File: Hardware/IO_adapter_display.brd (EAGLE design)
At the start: 67.3 x 41.9 mm, 23 parts, among them Y1 32Khz

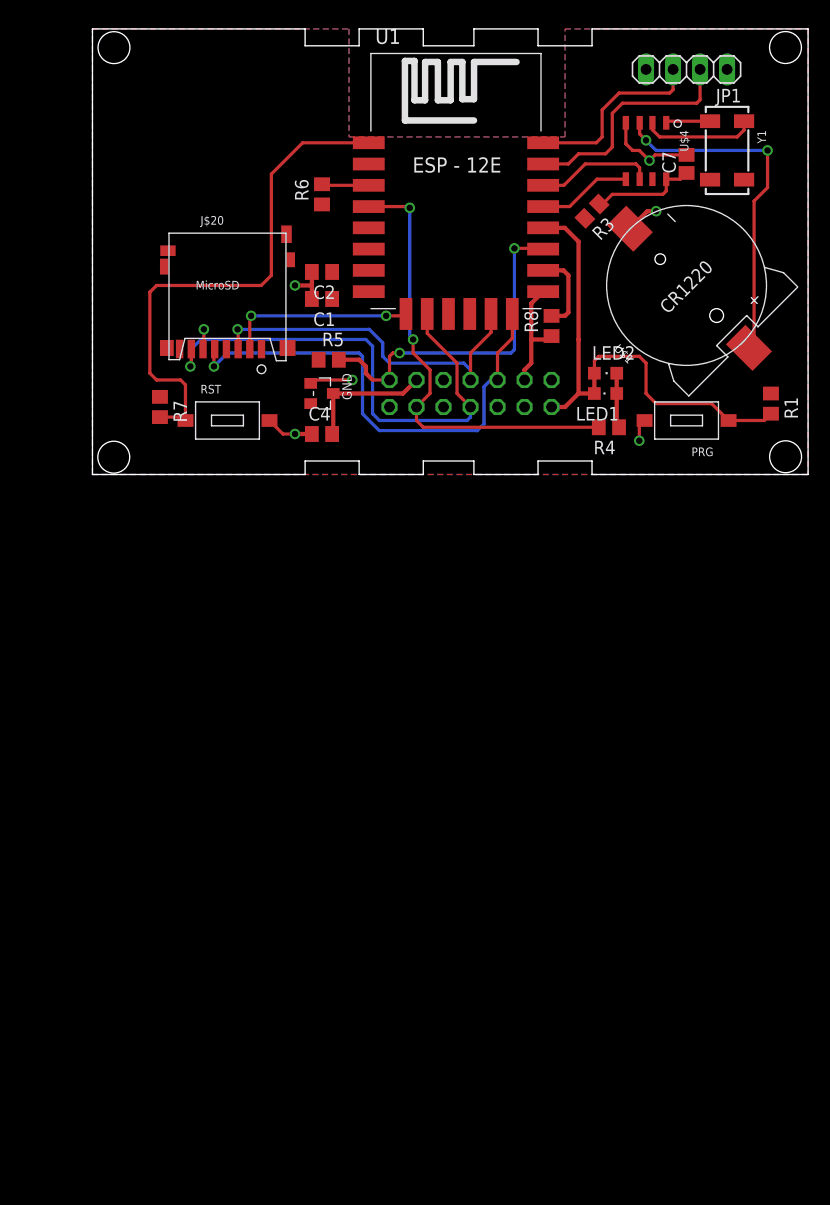
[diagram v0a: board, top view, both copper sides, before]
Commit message: beginning to add a 2.2" TFT display
not quite sure about the mechanical layout yet.
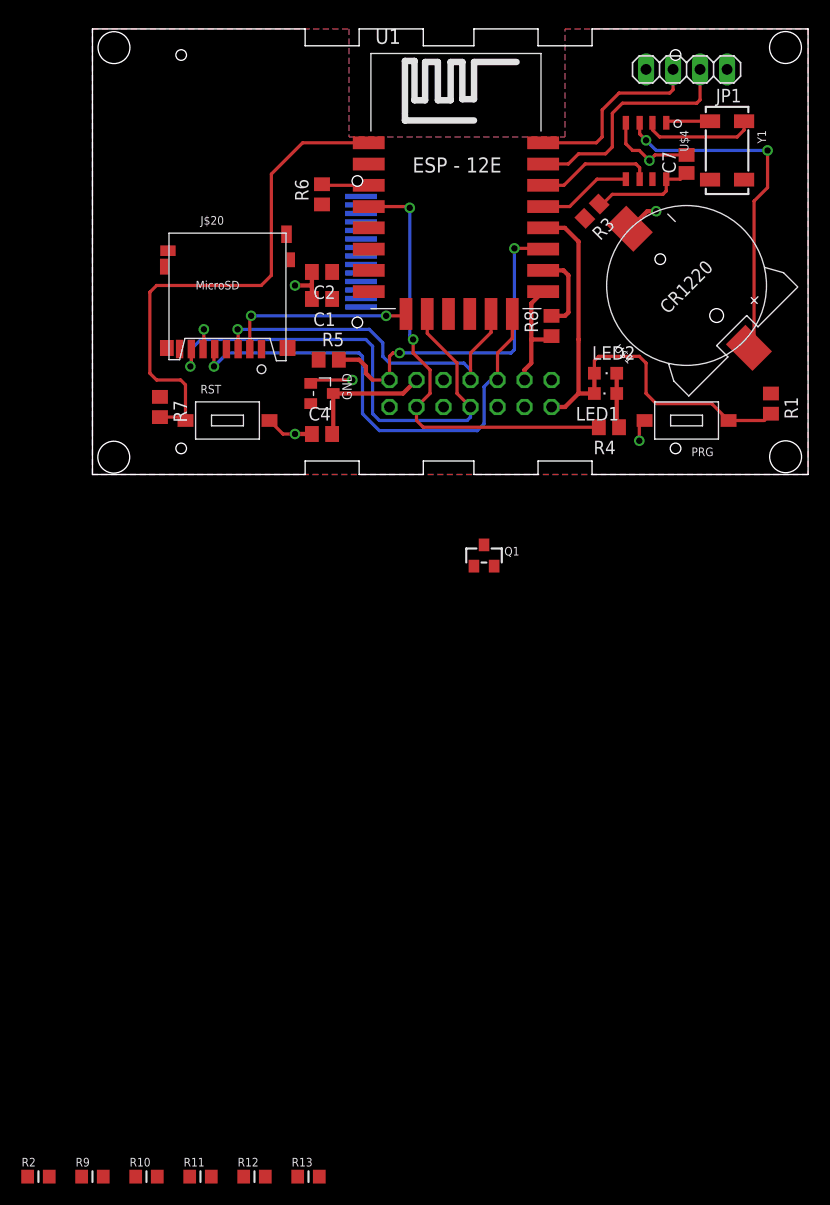
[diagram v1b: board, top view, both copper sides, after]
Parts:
- added Q1: 2N2222, microbuilder:SOT23-WIDE
- added R10, R13, R2, R9: 10, microbuilder:_0805MP
- added R11: 1K, microbuilder:_0805MP
- added R12: 10K, microbuilder:_0805MP
- added U2: (no value), microbuilder:TM022HDH26_2.2IN_LCD
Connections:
- new net 3.3V: R12.2, U2.10, U2.9
- new net BACKLIGHT: R11.1, R12.1
- new net DC_3V: U2.4
- new net LCDCS_3V: U2.5
- new net LEDK: Q1.3, R10.1, R13.1, R2.1, R9.1
- new net MOSI_3V: U2.6
- new net N$2: R2.2, U2.11
- new net N$3: R9.2, U2.12
- new net N$4: R10.2, U2.13
- new net N$5: Q1.1, R11.2
- new net N$6: R13.2, U2.14
- new net RESET_3V: U2.2
- new net SCLK_3V: U2.3
- net GND: now also Q1.2, U2.1, U2.8
- net MISO: now also U2.7
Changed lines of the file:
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@@
 <element name="RST" library="tactile_switch" package="TACT_6X3.5" value="6X3.5_TACT" x="12.7" y="5.08"/>
 <element name="JP1" library="pinhead" package="1X04" value="" x="55.88" y="38.1" rot="R180"/>
+<element name="R2" library="microbuilder" package="_0805MP" value="10" x="-5.08" y="-66.04"/>
+<element name="R9" library="microbuilder" package="_0805MP" value="10" x="0" y="-66.04"/>
+<element name="R10" library="microbuilder" package="_0805MP" value="10" x="5.08" y="-66.04"/>
+<element name="Q1" library="microbuilder" package="SOT23-WIDE" value="2N2222" x="36.83" y="-7.62"/>
+<element name="R11" library="microbuilder" package="_0805MP" value="1K" x="10.16" y="-66.04"/>
+<element name="R12" library="microbuilder" package="_0805MP" value="10K" x="15.24" y="-66.04"/>
+<element name="U2" library="microbuilder" package="TM022HDH26_2.2IN_LCD" value="" x="34.925" y="20.955" rot="MR90"/>
+<element name="R13" library="microbuilder" package="_0805MP" value="10" x="20.32" y="-66.04"/>
 </elements>
 <signals>
@@
 <wire x1="52.187690625" y1="24.765" x2="53.0225" y2="24.765" width="0.4064" layer="1"/>
 <via x="53.0225" y="24.765" extent="1-16" drill="0.6" shape="octagon"/>
-<wire x1="33.02" y1="6.35" x2="40.64" y2="6.35" width="0" layer="19" extent="1-1"/>
+<contactref element="U2" pad="1"/>
+<contactref element="U2" pad="8"/>
+<contactref element="Q1" pad="2"/>
+<wire x1="50.17" y1="33.08" x2="52.07" y2="38.1" width="0" layer="19" extent="1-1"/>
+<wire x1="52.187690625" y1="24.765" x2="52.3875" y2="29.5275" width="0" layer="19" extent="1-1"/>
+<wire x1="42.39" y1="17.2" x2="50.54134375" y2="23.118653125" width="0" layer="19" extent="1-1"/>
+<wire x1="40.64" y1="6.35" x2="40.64" y2="8.89" width="0" layer="19" extent="1-1"/>
+<wire x1="33.02" y1="8.89" x2="40.64" y2="8.89" width="0" layer="19" extent="1-1"/>
+<wire x1="33.02" y1="6.35" x2="33.02" y2="8.89" width="0" layer="19" extent="1-1"/>
+<wire x1="24.4475" y1="8.89" x2="33.02" y2="8.89" width="0" layer="19" extent="1-1"/>
+<wire x1="20.64" y1="3.81" x2="20.53" y2="8.57" width="0" layer="19" extent="1-1"/>
+<wire x1="20.64" y1="16.51" x2="20.85" y2="8.89" width="0" layer="19" extent="1-1"/>
+<wire x1="10.4775" y1="11.7225" x2="16.65" y2="5.08" width="0" layer="19" extent="1-1"/>
+<wire x1="51.435" y1="5.08" x2="40.64" y2="6.35" width="0" layer="19" extent="1-1"/>
+<wire x1="37.78" y1="-8.62" x2="40.64" y2="6.35" width="0" layer="19" extent="1-1"/>
+<wire x1="25.265" y1="21.355" x2="37.78" y2="-8.62" width="0" layer="19" extent="1-1"/>
+<wire x1="25.265" y1="15.755" x2="25.265" y2="21.355" width="0" layer="19" extent="1-1"/>
 </signal>
 <signal name="MISO">
@@
 <wire x1="9.3" y1="11.8" x2="9.3" y2="10.2525" width="0.3048" layer="16"/>
 <wire x1="9.3" y1="10.2525" x2="9.2075" y2="10.16" width="0.3048" layer="16"/>
+<contactref element="U2" pad="7"/>
+<wire x1="26.9875" y1="5.08" x2="25.265" y2="20.555" width="0" layer="19" extent="1-16"/>
 </signal>
 <signal name="MOSI">
@@
 </polygon>
 <contactref element="JP1" pad="1"/>
+<wire x1="46.318246875" y1="24.093246875" x2="59.69" y2="38.1" width="0" layer="19" extent="1-1"/>
+<wire x1="43.18" y1="8.89" x2="46.318246875" y2="24.093246875" width="0" layer="19" extent="1-1"/>
+<wire x1="25.99" y1="17.2" x2="43.18" y2="8.89" width="0" layer="19" extent="1-1"/>
+<wire x1="22.54" y1="16.51" x2="25.99" y2="17.2" width="0" layer="19" extent="1-1"/>
+<wire x1="22.54" y1="19.05" x2="22.54" y2="16.51" width="0" layer="19" extent="1-1"/>
+<wire x1="21.275" y1="10.795" x2="22.54" y2="16.51" width="0" layer="19" extent="1-1"/>
+<wire x1="20.53" y1="6.67" x2="21.275" y2="10.795" width="0" layer="19" extent="1-1"/>
+<wire x1="21.59" y1="25.4025" x2="22.54" y2="19.05" width="0" layer="19" extent="1-1"/>
+<wire x1="12.6" y1="11.8" x2="21.275" y2="10.795" width="0" layer="19" extent="1-1"/>
+<wire x1="6.35" y1="7.3" x2="12.6" y2="11.8" width="0" layer="19" extent="1-1"/>
+<wire x1="63.8175" y1="7.6175" x2="43.18" y2="8.89" width="0" layer="19" extent="1-1"/>
 </signal>
 <signal name="ADCCS1">
@@
 <wire x1="53.97" y1="26.665" x2="53.97" y2="27.78" width="0.3048" layer="1"/>
 </signal>
+<signal name="LEDK">
+<contactref element="R2" pad="1"/>
+<contactref element="R10" pad="1"/>
+<contactref element="R9" pad="1"/>
+<contactref element="Q1" pad="3"/>
+<contactref element="R13" pad="1"/>
+<wire x1="-1.016" y1="-66.04" x2="-6.096" y2="-66.04" width="0" layer="19" extent="1-1"/>
+<wire x1="4.064" y1="-66.04" x2="-1.016" y2="-66.04" width="0" layer="19" extent="1-1"/>
+<wire x1="19.304" y1="-66.04" x2="4.064" y2="-66.04" width="0" layer="19" extent="1-1"/>
+<wire x1="36.83" y1="-6.62" x2="19.304" y2="-66.04" width="0" layer="19" extent="1-1"/>
+</signal>
+<signal name="N$2">
+<contactref element="R2" pad="2"/>
+<contactref element="U2" pad="11"/>
+<wire x1="25.265" y1="23.755" x2="-4.064" y2="-66.04" width="0" layer="19" extent="1-1"/>
+</signal>
+<signal name="N$3">
+<contactref element="R9" pad="2"/>
+<contactref element="U2" pad="12"/>
+<wire x1="25.265" y1="24.555" x2="1.016" y2="-66.04" width="0" layer="19" extent="1-1"/>
+</signal>
+<signal name="N$4">
+<contactref element="R10" pad="2"/>
+<contactref element="U2" pad="13"/>
+<wire x1="25.265" y1="25.355" x2="6.096" y2="-66.04" width="0" layer="19" extent="1-1"/>
+</signal>
+<signal name="3.3V">
+<contactref element="R12" pad="2"/>
+<contactref element="U2" pad="10"/>
+<contactref element="U2" pad="9"/>
+<wire x1="25.265" y1="22.955" x2="16.256" y2="-66.04" width="0" layer="19" extent="1-1"/>
+<wire x1="25.265" y1="22.155" x2="25.265" y2="22.955" width="0" layer="19" extent="1-1"/>
+</signal>
+<signal name="RESET_3V">
+<contactref element="U2" pad="2"/>
+</signal>
+<signal name="SCLK_3V">
+<contactref element="U2" pad="3"/>
+</signal>
+<signal name="MOSI_3V">
+<contactref element="U2" pad="6"/>
+</signal>
+<signal name="LCDCS_3V">
+<contactref element="U2" pad="5"/>
+</signal>
+<signal name="BACKLIGHT">
+<contactref element="R11" pad="1"/>
+<contactref element="R12" pad="1"/>
+<wire x1="14.224" y1="-66.04" x2="9.144" y2="-66.04" width="0" layer="19" extent="1-1"/>
+</signal>
+<signal name="N$5">
+<contactref element="R11" pad="2"/>
+<contactref element="Q1" pad="1"/>
+<wire x1="35.88" y1="-8.62" x2="11.176" y2="-66.04" width="0" layer="19" extent="1-1"/>
+</signal>
+<signal name="DC_3V">
+<contactref element="U2" pad="4"/>
+</signal>
+<signal name="N$6">
+<contactref element="R13" pad="2"/>
+<contactref element="U2" pad="14"/>
+<wire x1="25.265" y1="26.155" x2="21.336" y2="-66.04" width="0" layer="19" extent="1-1"/>
+</signal>
 </signals>
